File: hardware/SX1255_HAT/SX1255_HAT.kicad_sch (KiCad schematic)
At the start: 32 parts, among them IC1 SX1255, J1 TX_SMA, J2 RX_SMA, J3 RPi Zero, Y1 32MHz

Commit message: Added Tx filters, EEPROM, modified for soapy-sx compat
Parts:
- added C14, C15: 6.8p, Capacitor_SMD:C_0603_1608Metric, symbol Device:C_Small
- added JP1: RST_SEL, Jumper:SolderJumper-3_P1.3mm_Bridged12_RoundedPad1.0x1.5mm_NumberLabels, symbol Jumper:Jumper_3_Bridged12
- added L3: 33n, Inductor_SMD:L_0603_1608Metric, symbol Device:L_Small
- added R8, R9: 3K9, Resistor_SMD:R_0603_1608Metric, symbol Device:R_Small
- added U1: 24LC256, Package_SO:SOIC-8_3.9x4.9mm_P1.27mm, symbol Memory_EEPROM:24LC256
- J1: value TX_SMA -> TX; footprint Connector_Coaxial:SMA_Amphenol_901-144_Vertical -> Connector_Coaxial:U.FL_Molex_MCRF_73412-0110_Vertical
- J2: value RX_SMA -> RX; footprint Connector_Coaxial:SMA_Amphenol_901-144_Vertical -> Connector_Coaxial:U.FL_Molex_MCRF_73412-0110_Vertical
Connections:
- net +3V3: now also R8.1, R9.1, U1.8 (VCC)
- net GND: now also C14.2, C15.2, U1.1 (A0), U1.2 (A1), U1.3 (A2), U1.4 (GND)
- net RST: now also JP1.2 (C); no longer J3.22 (Pin_22)
- net at C11.2: now also C15.1, L3.1; no longer J1.1 (In)
- net ID_SD: now reaches J3.27 (Pin_27)
- net ID_SD: now also R9.2, U1.5 (SDA)
- net ID_SC: now reaches J3.28 (Pin_28)
- net ID_SC: now also R8.2, U1.6 (SCL)
- net GPIO5: now reaches J3.29 (Pin_29)
- net GPIO5: now also JP1.1 (A)
- new net: C14.1, J1.1 (In), L3.2
- new net GPIO25: J3.22 (Pin_22), JP1.3 (B)
- no-connect marks 36 -> 34
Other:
- moved on the sheet: C11, J1

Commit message: Added decoupling for EEPROM and WP pin
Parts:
- added C16: 10n, Capacitor_SMD:C_0603_1608Metric, symbol Device:C_Small
- added JP2: WP, Jumper:SolderJumper-2_P1.3mm_Open_RoundedPad1.0x1.5mm, symbol Jumper:Jumper_2_Open
- added R10: 3K9, Resistor_SMD:R_0603_1608Metric, symbol Device:R_Small
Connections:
- net +3V3: now also C16.1, R10.2
- net GND: now also C16.2, JP2.2 (B)
- net at U1.7 (WP): now also JP2.1 (A), R10.1
- no-connect marks 34 -> 33

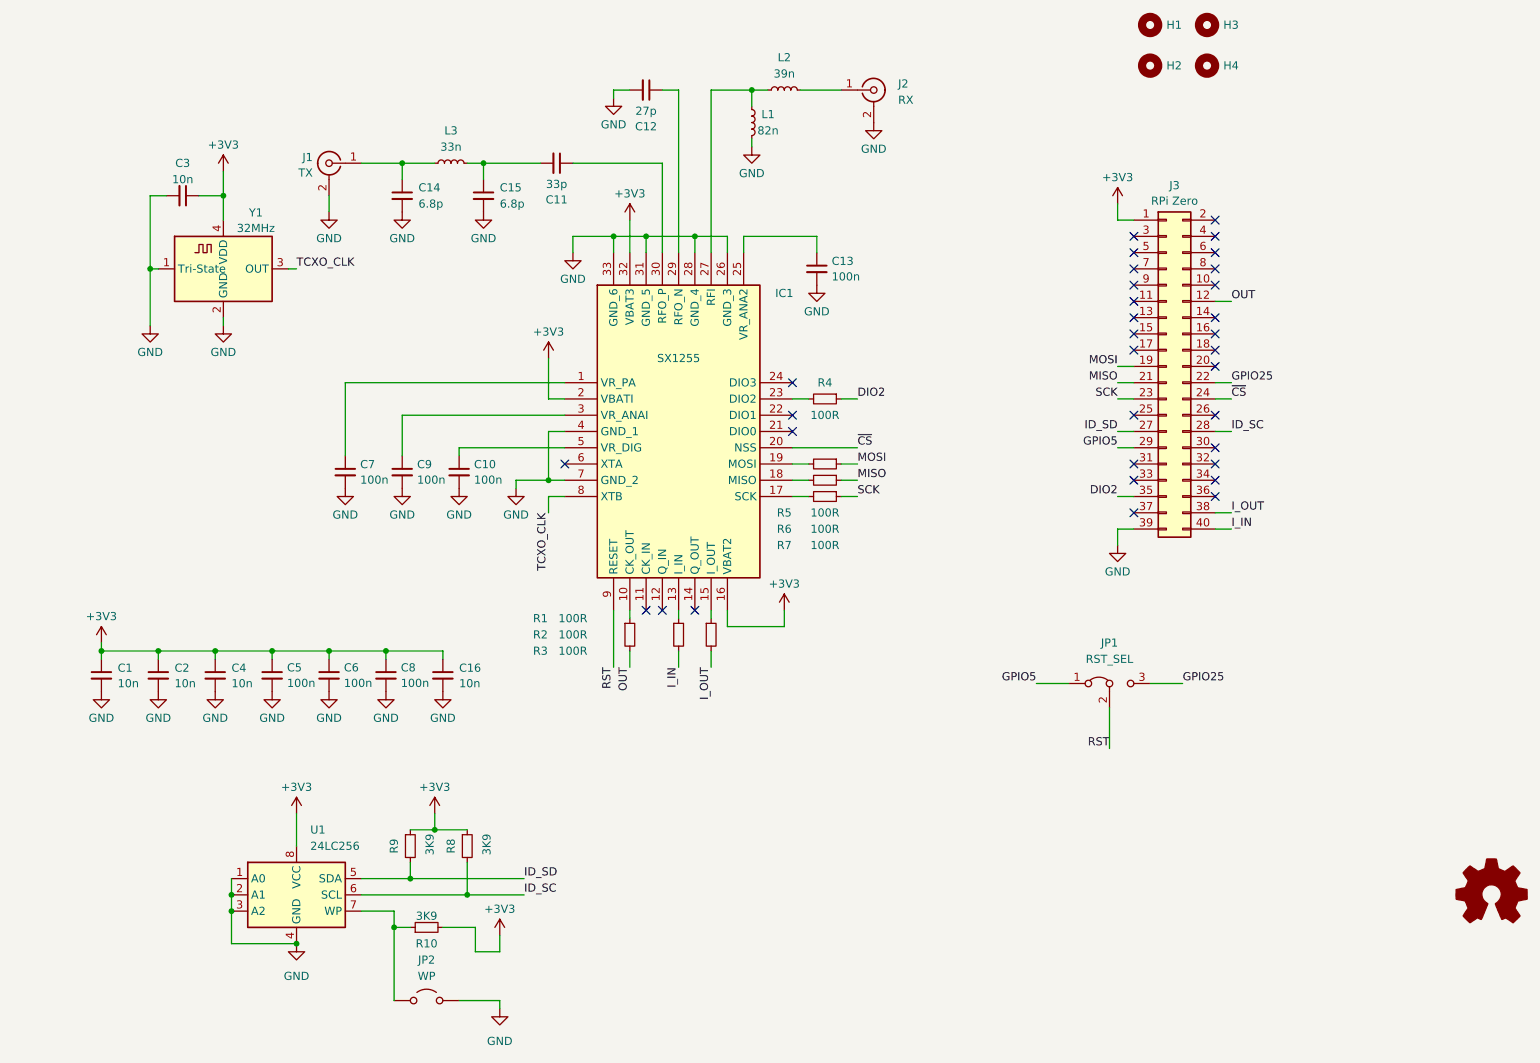
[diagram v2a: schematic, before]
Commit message: added DRU, modified component placement, updated schematic
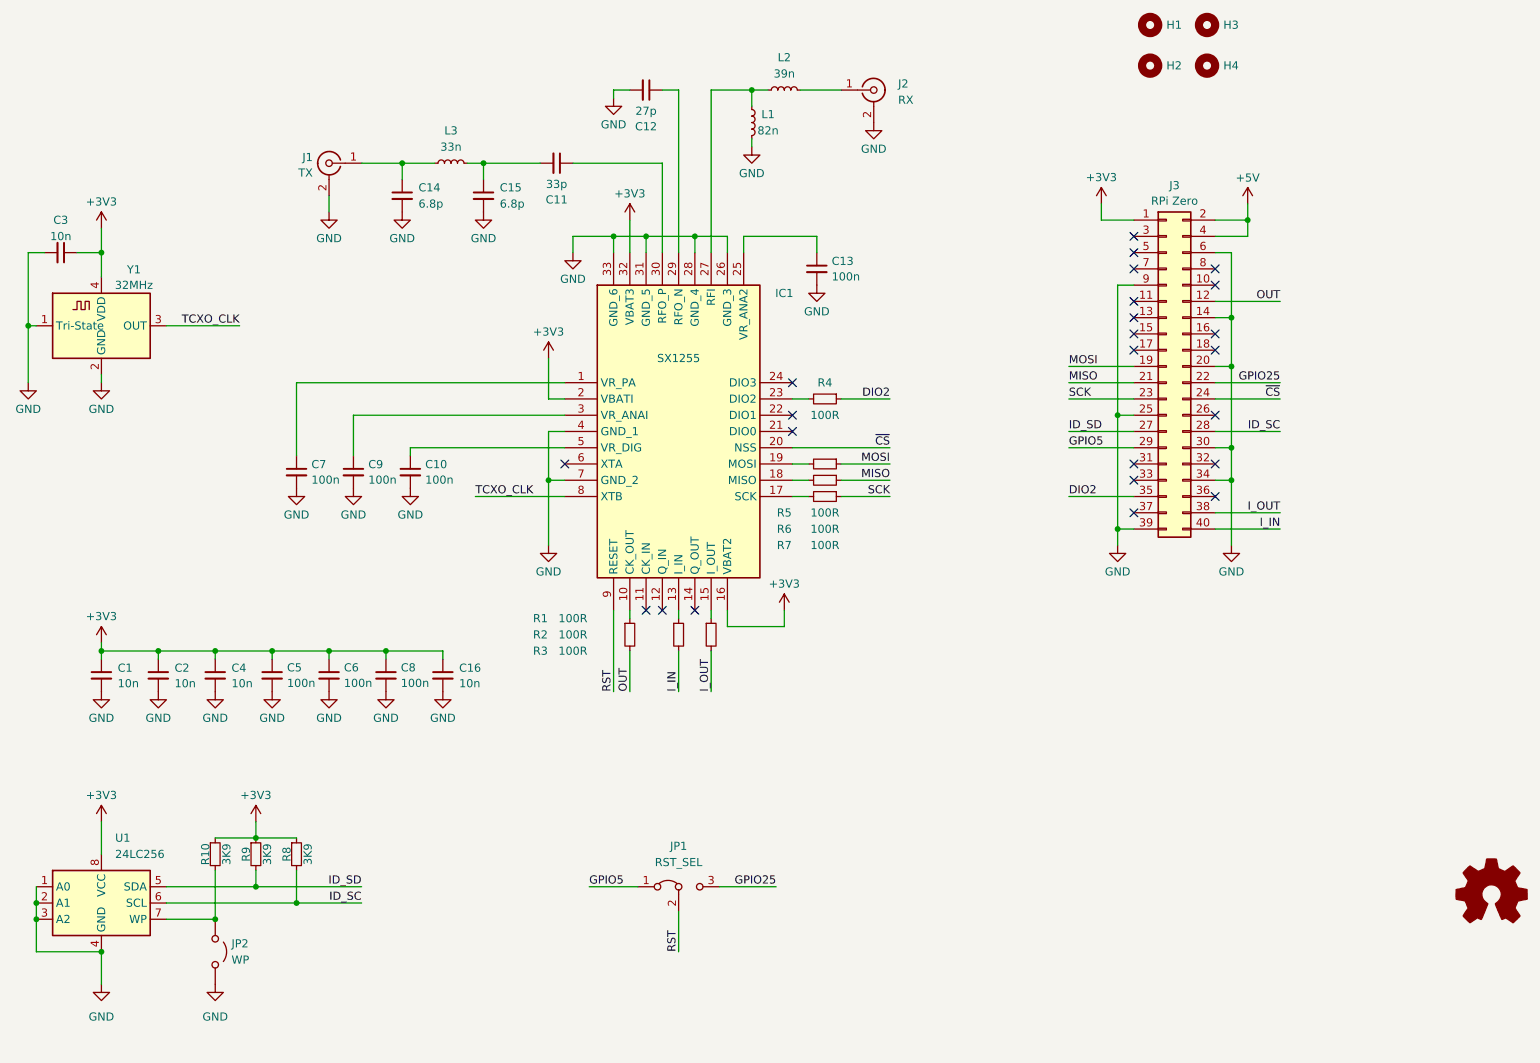
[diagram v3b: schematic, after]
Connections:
- net +3V3: now also R10.1; no longer R10.2
- net GND: now also J3.14 (Pin_14), J3.20 (Pin_20), J3.25 (Pin_25), J3.30 (Pin_30), J3.34 (Pin_34), J3.6 (Pin_6), J3.9 (Pin_9)
- net at JP2.1 (A), U1.7 (WP): now also R10.2; no longer R10.1
- net +5V: now reaches J3.2 (Pin_2)
- net +5V: now also J3.4 (Pin_4)
- no-connect marks 33 -> 24
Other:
- company: Jankyneering -> jankyneering.cc
- moved on the sheet: C10, C3, C7, C9, JP1, JP2, R10, R8, R9, U1, Y1
